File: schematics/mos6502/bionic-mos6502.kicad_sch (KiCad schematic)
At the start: 8 parts, among them J1 Bionic-P135, J2 Bionic-P245, U1 W65C816S, U2 11AA010-I/TT

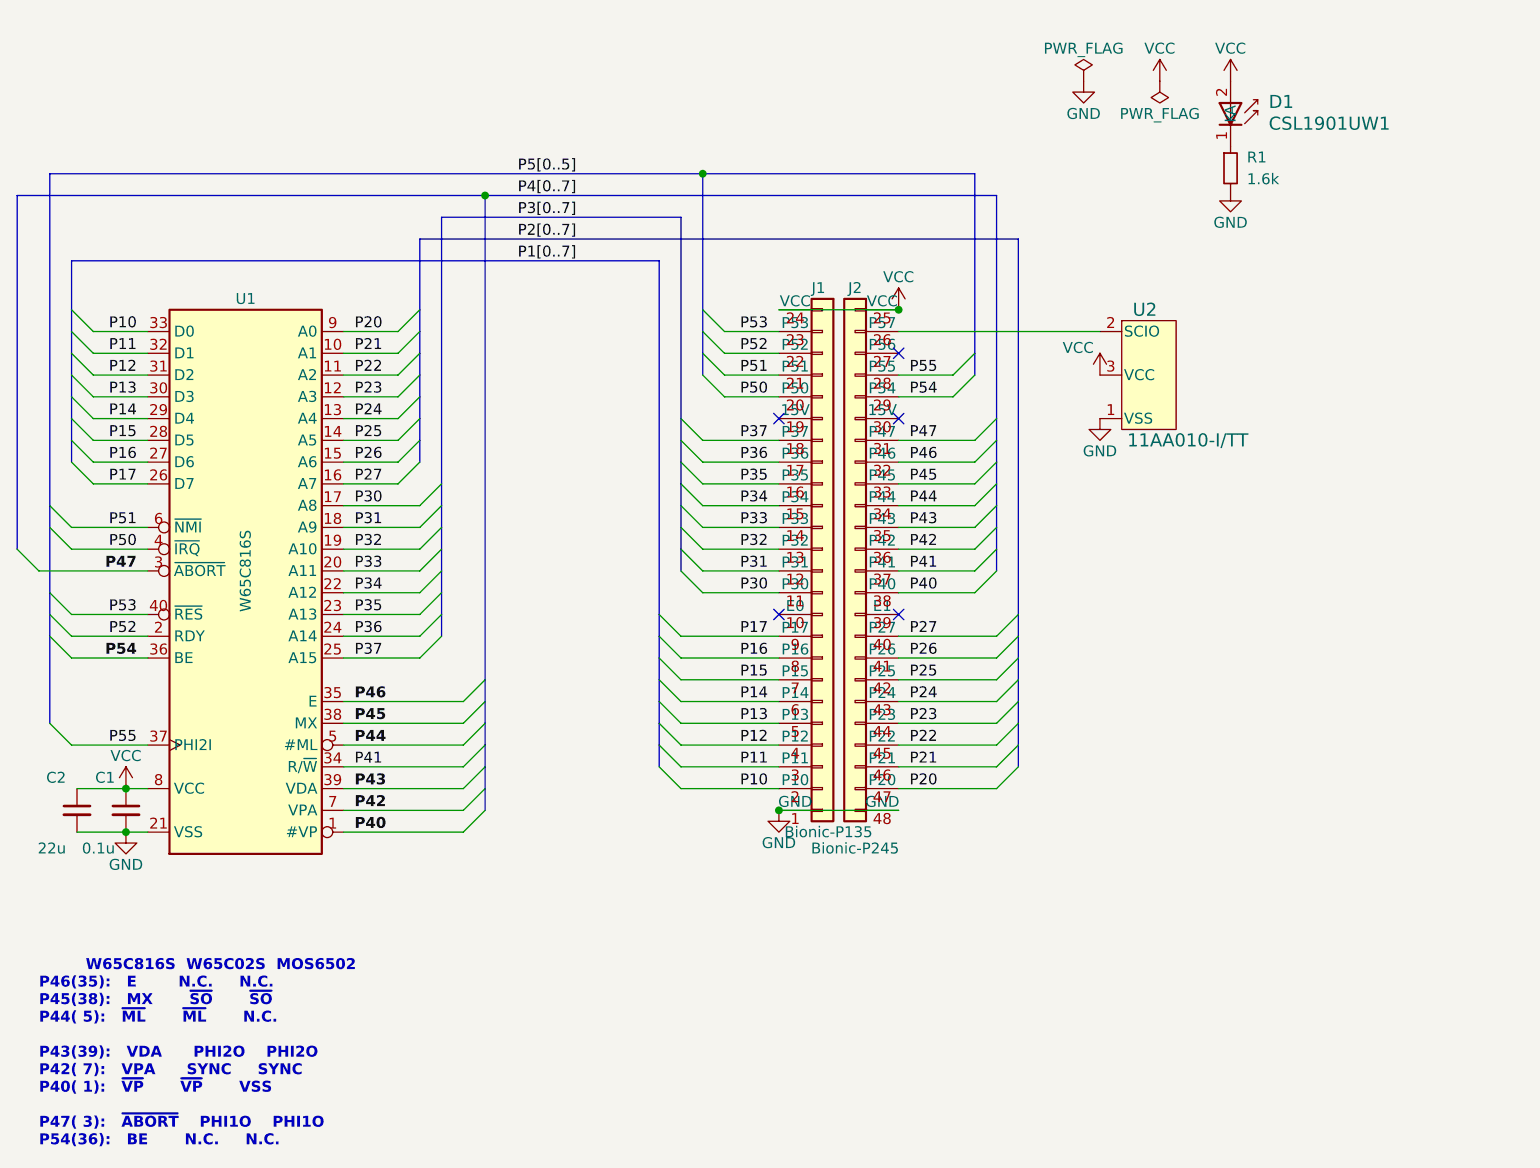
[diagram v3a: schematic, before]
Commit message: [MOS6502] Fix EEPROM pinout
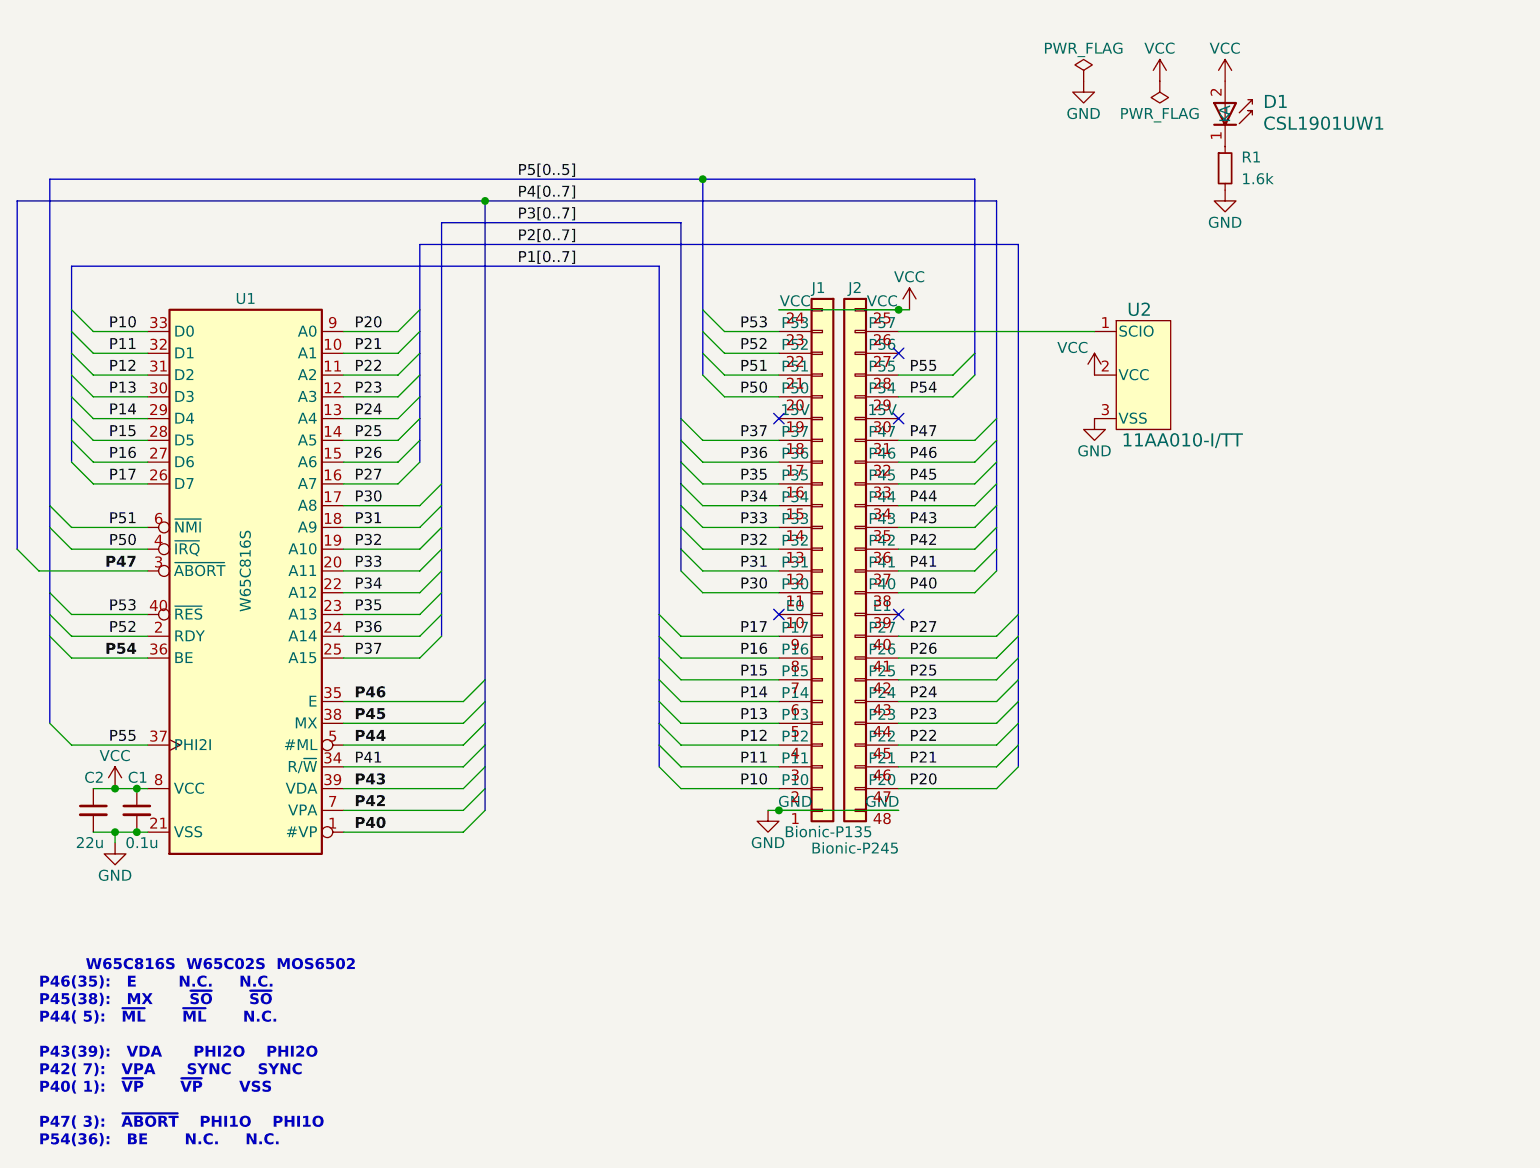
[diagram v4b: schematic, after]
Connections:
- net GND: now also U2.3 (VSS); no longer U2.1 (VSS)
- net VCC: now also U2.2 (VCC); no longer U2.3 (VCC)
- net at J2.26 (P57): now also U2.1 (SCIO); no longer U2.2 (SCIO)
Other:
- moved on the sheet: C1, C2, D1, R1, U2

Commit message: [schematics] Update LED footprint
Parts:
- D1: footprint 0-LocalLibrary:LED_CSL1901UW1_ROM -> 0-LocalLibrary:LED_CSL1901UW1_ROM-M

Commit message: [MOS6502] Cleanup schematics
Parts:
- D1: footprint 0-LocalLibrary:LED_CSL1901UW1_ROM-M -> rhom:LED_CSL1901UW1_ROM-M; symbol 0-LocalLibrary:CSL1901UW1 -> rhom:CSL1901UW1
- J1: footprint 0-LocalLibrary:Bionic-P135_Vertical -> bionic:Bionic-P135_Vertical; symbol 0-LocalLibrary:Bionic-P135 -> bionic:Bionic-P135
- J2: footprint 0-LocalLibrary:Bionic-P245_Vertical -> bionic:Bionic-P245_Vertical; symbol 0-LocalLibrary:Bionic-P245 -> bionic:Bionic-P245
- U1: footprint 0-LocalLibrary:DIP-40_W15.24mm_Socket -> bionic:DIP-40_W15.24mm_Socket; symbol 0-LocalLibrary:W65C816S -> cpu:W65C816S
- U2: footprint 0-LocalLibrary:SOT-23_MC_MCH-M -> microchip:SOT-23_MC_MCH-M; symbol 0-LocalLibrary:11AA010-I_TT -> microchip:11AA010-I_TT
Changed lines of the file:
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@@
 	)
 	(symbol
-		(lib_id "0-LocalLibrary:W65C816S")
+		(lib_id "cpu:W65C816S")
 		(at 83.82 100.33 0)
 		(unit 1)
@@
 			)
 		)
-		(property "Footprint" "0-LocalLibrary:DIP-40_W15.24mm_Socket"
+		(property "Footprint" "bionic:DIP-40_W15.24mm_Socket"
 			(at 82.55 134.62 0)
 			(effects
@@
 			)
 		)
-		(property "Description" ""
+		(property "Description" "8-bit General Purpose Microprocessor, DIP-40"
 			(at 83.82 100.33 0)
 			(effects
@@
 	)
 	(symbol
-		(lib_id "0-LocalLibrary:Bionic-P245")
+		(lib_id "bionic:Bionic-P245")
 		(at 158.75 97.79 0)
 		(unit 1)
@@
 			)
 		)
-		(property "Footprint" "0-LocalLibrary:Bionic-P245_Vertical"
+		(property "Footprint" "bionic:Bionic-P245_Vertical"
 			(at 160.02 133.35 0)
 			(effects
@@
 			)
 		)
-		(property "Description" ""
+		(property "Description" "Generic connector, single row, 01x24, script generated (kicad-library-utils/schlib/autogen/connector/)"
 			(at 158.75 97.79 0)
 			(effects
@@
 	)
 	(symbol
-		(lib_id "0-LocalLibrary:CSL1901UW1")
+		(lib_id "rhom:CSL1901UW1")
 		(at 198.12 43.18 270)
 		(unit 1)
@@
 		(fields_autoplaced yes)
 		(property "Reference" "D1"
-			(at 202.565 45.593 90)
+			(at 201.93 45.5929 90)
 			(effects
 				(font
@@
 		)
 		(property "Value" "CSL1901UW1"
-			(at 202.565 48.133 90)
+			(at 201.93 48.1329 90)
 			(effects
 				(font
@@
 			)
 		)
-		(property "Footprint" "0-LocalLibrary:LED_CSL1901UW1_ROM-M"
+		(property "Footprint" "rhom:LED_CSL1901UW1_ROM-M"
 			(at 189.23 46.99 0)
 			(effects
@@
 	)
 	(symbol
-		(lib_id "0-LocalLibrary:Bionic-P135")
+		(lib_id "bionic:Bionic-P135")
 		(at 151.13 97.79 0)
 		(unit 1)
@@
 			)
 		)
-		(property "Footprint" "0-LocalLibrary:Bionic-P135_Vertical"
+		(property "Footprint" "bionic:Bionic-P135_Vertical"
 			(at 152.4 133.35 0)
 			(effects
@@
 			)
 		)
-		(property "Description" ""
+		(property "Description" "Generic connector, single row, 01x24, script generated (kicad-library-utils/schlib/autogen/connector/)"
 			(at 151.13 97.79 0)
 			(effects
@@
 	)
 	(symbol
-		(lib_id "0-LocalLibrary:11AA010-I_TT")
+		(lib_id "microchip:11AA010-I_TT")
 		(at 185.42 71.12 0)
 		(unit 1)
@@
 			)
 		)
-		(property "Footprint" "0-LocalLibrary:SOT-23_MC_MCH-M"
+		(property "Footprint" "microchip:SOT-23_MC_MCH-M"
 			(at 187.96 88.9 0)
 			(effects
@@
 			)
 		)
-		(property "Description" ""
+		(property "Description" "UNI/O Serial EEPROM (1Kbit)"
 			(at 185.42 71.12 0)
 			(effects

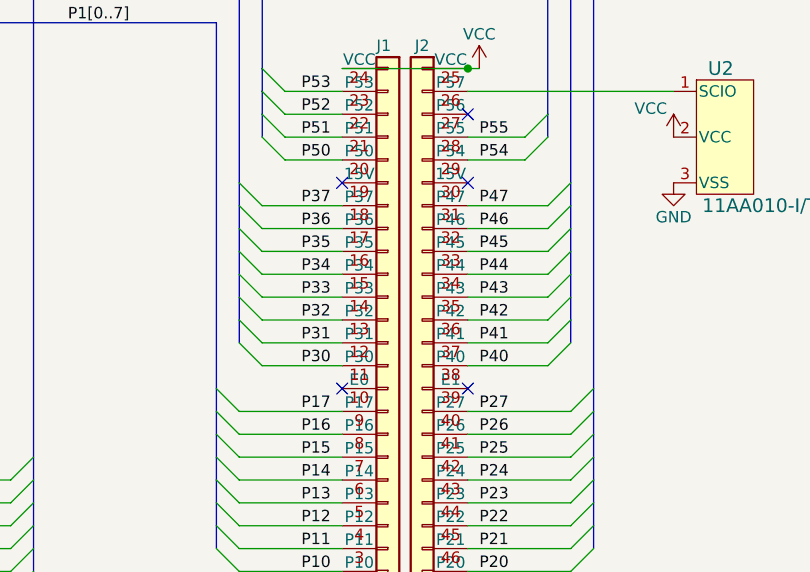
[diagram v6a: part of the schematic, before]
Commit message: [MOS6502] Update schematics
Remove unused pins from bionic connector
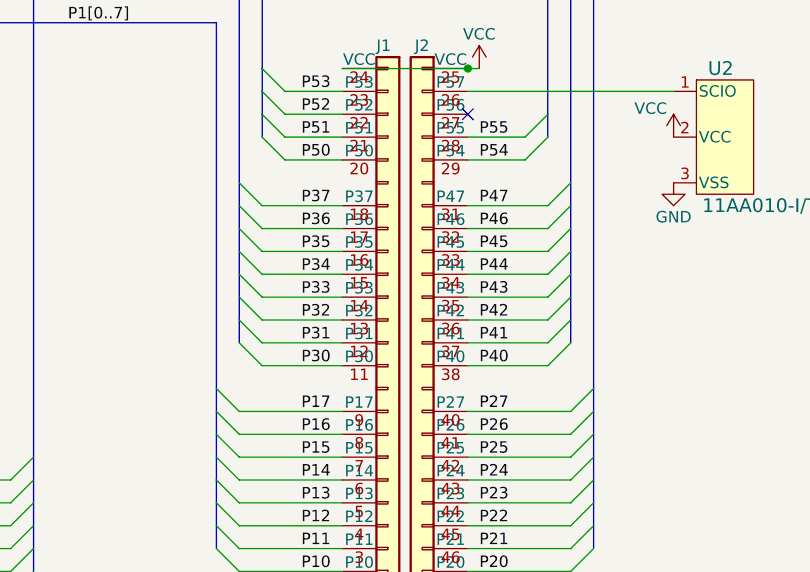
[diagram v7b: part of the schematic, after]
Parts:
- J1: footprint bionic:Bionic-P135_Vertical -> bionic:Bionic-P135_THT
- J2: footprint bionic:Bionic-P245_Vertical -> bionic:Bionic-P245_THT
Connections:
- no-connect marks 5 -> 1
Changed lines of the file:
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@@
 	(title_block
 		(title "BionicMOS6502")
-		(date "2024-11-01")
-		(rev "9")
+		(date "2025-03-02")
+		(rev "10")
 		(company "Tadashi G. Takaoka")
 	)
@@
 	)
 	(no_connect
-		(at 160.02 105.41)
-	)
-	(no_connect
 		(at 160.02 74.93)
 	)
-	(no_connect
-		(at 146.05 105.41)
-	)
-	(no_connect
-		(at 160.02 82.55)
-	)
-	(no_connect
-		(at 146.05 82.55)
-	)
 	(bus_entry
 		(at 60.96 107.95)
@@
 			)
 		)
-		(property "Footprint" "bionic:Bionic-P245_Vertical"
+		(property "Footprint" "bionic:Bionic-P245_THT"
 			(at 160.02 133.35 0)
 			(effects
@@
 		(pin "26"
 		)
-		(pin "39"
-		)
 		(pin "36"
 		)
 		(pin "37"
 		)
-		(pin "30"
-		)
 		(pin "29"
 		)
@@
 			)
 		)
-		(property "Footprint" "bionic:Bionic-P135_Vertical"
+		(property "Footprint" "bionic:Bionic-P135_THT"
 			(at 152.4 133.35 0)
 			(effects
@@
 		(pin "24"
 		)
-		(pin "19"
-		)
 		(pin "16"
 		)
@@
 		(pin "21"
 		)
-		(pin "10"
-		)
 		(pin "13"
